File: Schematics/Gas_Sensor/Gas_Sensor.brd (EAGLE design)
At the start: 46.7 x 45.7 mm, 9 parts, among them J1 RJ45, X1 GAS_SENSOR

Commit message: Layout for final inspection
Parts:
- C1, C2: value (none) -> 0.1uF
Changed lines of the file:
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@@
 <layer number="25" name="tNames" color="7" fill="1" visible="yes" active="yes"/>
 <layer number="26" name="bNames" color="7" fill="1" visible="yes" active="yes"/>
-<layer number="27" name="tValues" color="7" fill="1" visible="yes" active="yes"/>
+<layer number="27" name="tValues" color="7" fill="1" visible="no" active="yes"/>
 <layer number="28" name="bValues" color="7" fill="1" visible="yes" active="yes"/>
 <layer number="29" name="tStop" color="7" fill="3" visible="no" active="yes"/>
@@
 </class>
 </classes>
-<designrules name="default">
+<designrules name="LaenPCBOrder">
 <description language="de">&lt;b&gt;EAGLE Design Rules&lt;/b&gt;
 &lt;p&gt;
@@
 Einstellungen hier und speichern die Design Rules unter
 einem neuen Namen ab.</description>
-<description language="en">&lt;b&gt;EAGLE Design Rules&lt;/b&gt;
+<description language="en">&lt;b&gt;Laen's PCB Order Design Rules&lt;/b&gt;
 &lt;p&gt;
-The default Design Rules have been set to cover
-a wide range of applications. Your particular design
-may have different requirements, so please make the
-necessary adjustments and save your customized
-design rules under a new name.</description>
+Please make sure your boards conform to these design rules.</description>
 <param name="layerSetup" value="(1*16)"/>
-<param name="mtCopper" value="0.035mm 0.035mm 0.035mm 0.035mm 0.035mm 0.035mm 0.035mm 0.035mm 0.035mm 0.035mm 0.035mm 0.035mm 0.035mm 0.035mm 0.035mm 0.035mm"/>
-<param name="mtIsolate" value="1.5mm 0.15mm 0.2mm 0.15mm 0.2mm 0.15mm 0.2mm 0.15mm 0.2mm 0.15mm 0.2mm 0.15mm 0.2mm 0.15mm 0.2mm"/>
-<param name="mdWireWire" value="8mil"/>
-<param name="mdWirePad" value="8mil"/>
-<param name="mdWireVia" value="8mil"/>
-<param name="mdPadPad" value="8mil"/>
-<param name="mdPadVia" value="8mil"/>
-<param name="mdViaVia" value="8mil"/>
-<param name="mdSmdPad" value="8mil"/>
-<param name="mdSmdVia" value="8mil"/>
-<param name="mdSmdSmd" value="8mil"/>
+<param name="mtCopper" value="0.0356mm 0.0356mm 0.0356mm 0.0356mm 0.0356mm 0.0356mm 0.0356mm 0.0356mm 0.0356mm 0.0356mm 0.0356mm 0.0356mm 0.0356mm 0.0356mm 0.0356mm 0.0356mm"/>
+<param name="mtIsolate" value="1.5011mm 0.1499mm 0.2007mm 0.1499mm 0.2007mm 0.1499mm 0.2007mm 0.1499mm 0.2007mm 0.1499mm 0.2007mm 0.1499mm 0.2007mm 0.1499mm 0.2007mm"/>
+<param name="mdWireWire" value="6mil"/>
+<param name="mdWirePad" value="6mil"/>
+<param name="mdWireVia" value="6mil"/>
+<param name="mdPadPad" value="6mil"/>
+<param name="mdPadVia" value="6mil"/>
+<param name="mdViaVia" value="6mil"/>
+<param name="mdSmdPad" value="6mil"/>
+<param name="mdSmdVia" value="6mil"/>
+<param name="mdSmdSmd" value="6mil"/>
 <param name="mdViaViaSameLayer" value="8mil"/>
 <param name="mnLayersViaInSmd" value="2"/>
-<param name="mdCopperDimension" value="40mil"/>
-<param name="mdDrill" value="8mil"/>
+<param name="mdCopperDimension" value="15mil"/>
+<param name="mdDrill" value="6mil"/>
 <param name="mdSmdStop" value="0mil"/>
-<param name="msWidth" value="10mil"/>
-<param name="msDrill" value="24mil"/>
-<param name="msMicroVia" value="9.99mm"/>
+<param name="msWidth" value="6mil"/>
+<param name="msDrill" value="13mil"/>
+<param name="msMicroVia" value="13mil"/>
 <param name="msBlindViaRatio" value="0.5"/>
 <param name="rvPadTop" value="0.25"/>
@@
 <param name="rvMicroViaOuter" value="0.25"/>
 <param name="rvMicroViaInner" value="0.25"/>
-<param name="rlMinPadTop" value="10mil"/>
+<param name="rlMinPadTop" value="7mil"/>
 <param name="rlMaxPadTop" value="20mil"/>
-<param name="rlMinPadInner" value="10mil"/>
+<param name="rlMinPadInner" value="7mil"/>
 <param name="rlMaxPadInner" value="20mil"/>
-<param name="rlMinPadBottom" value="10mil"/>
+<param name="rlMinPadBottom" value="7mil"/>
 <param name="rlMaxPadBottom" value="20mil"/>
-<param name="rlMinViaOuter" value="8mil"/>
+<param name="rlMinViaOuter" value="7mil"/>
 <param name="rlMaxViaOuter" value="20mil"/>
-<param name="rlMinViaInner" value="8mil"/>
+<param name="rlMinViaInner" value="7mil"/>
 <param name="rlMaxViaInner" value="20mil"/>
 <param name="rlMinMicroViaOuter" value="4mil"/>
@@
 <param name="mvStopFrame" value="1"/>
 <param name="mvCreamFrame" value="0"/>
-<param name="mlMinStopFrame" value="4mil"/>
-<param name="mlMaxStopFrame" value="4mil"/>
+<param name="mlMinStopFrame" value="3mil"/>
+<param name="mlMaxStopFrame" value="3mil"/>
 <param name="mlMinCreamFrame" value="0mil"/>
 <param name="mlMaxCreamFrame" value="0mil"/>
@@
 <element name="H2" library="holes" package="2,8" value="MOUNT-HOLE2.8" x="5.08" y="74.93"/>
 <element name="H3" library="holes" package="2,8" value="MOUNT-HOLE2.8" x="41.91" y="74.93"/>
-<element name="C1" library="rcl" package="C0603K" value="" x="24.765" y="59.055" smashed="yes">
+<element name="C1" library="rcl" package="C0603K" value="0.1uF" x="24.765" y="59.055" smashed="yes">
 <attribute name="NAME" x="26.505" y="57.8" size="1.016" layer="25"/>
 <attribute name="VALUE" x="23.965" y="57.405" size="1.016" layer="27"/>
 </element>
-<element name="C2" library="rcl" package="C0603K" value="" x="24.765" y="55.88" smashed="yes">
+<element name="C2" library="rcl" package="C0603K" value="0.1uF" x="24.765" y="55.88" smashed="yes">
 <attribute name="NAME" x="26.505" y="54.625" size="1.016" layer="25"/>
 <attribute name="VALUE" x="23.965" y="54.23" size="1.016" layer="27"/>

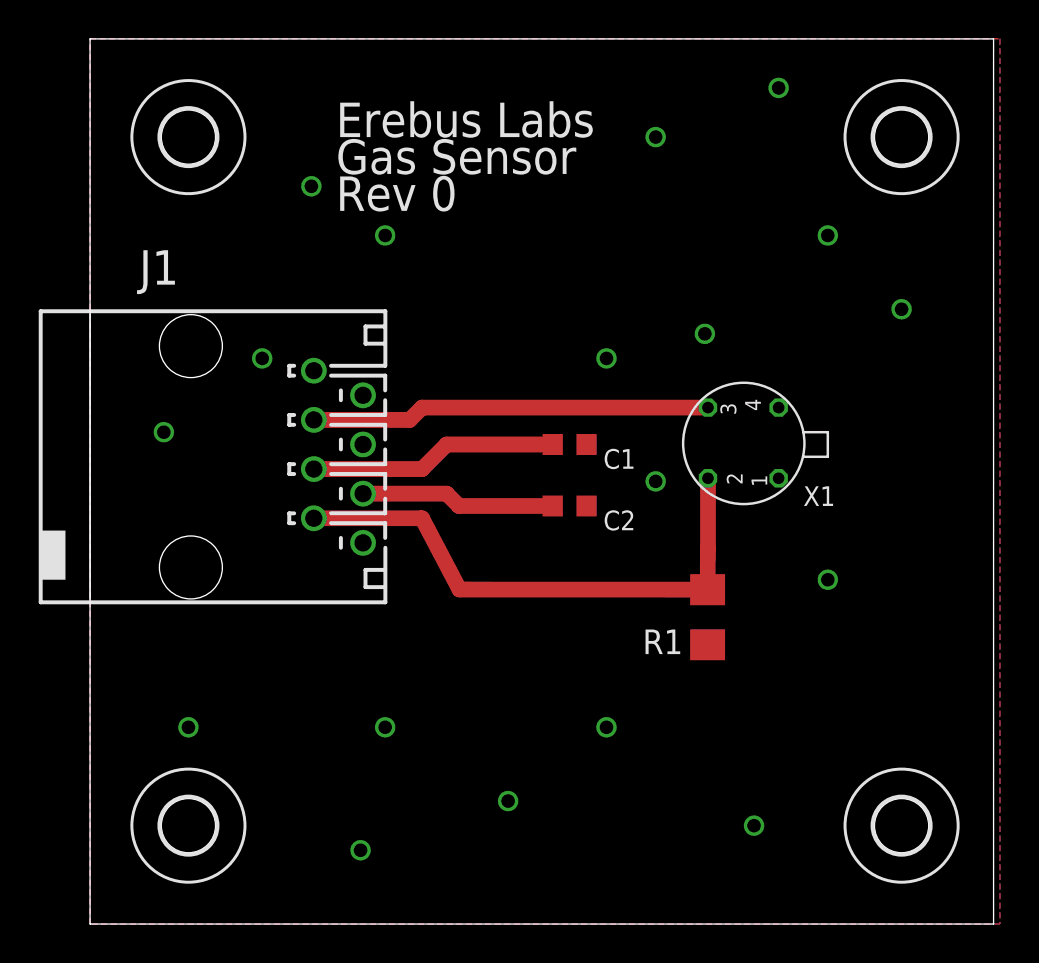
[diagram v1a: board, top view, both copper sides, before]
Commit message: Cleaned up stuff
Made Schematics easier to read
Split Supplies in BOM and made names match references
Renamed parts on sensor
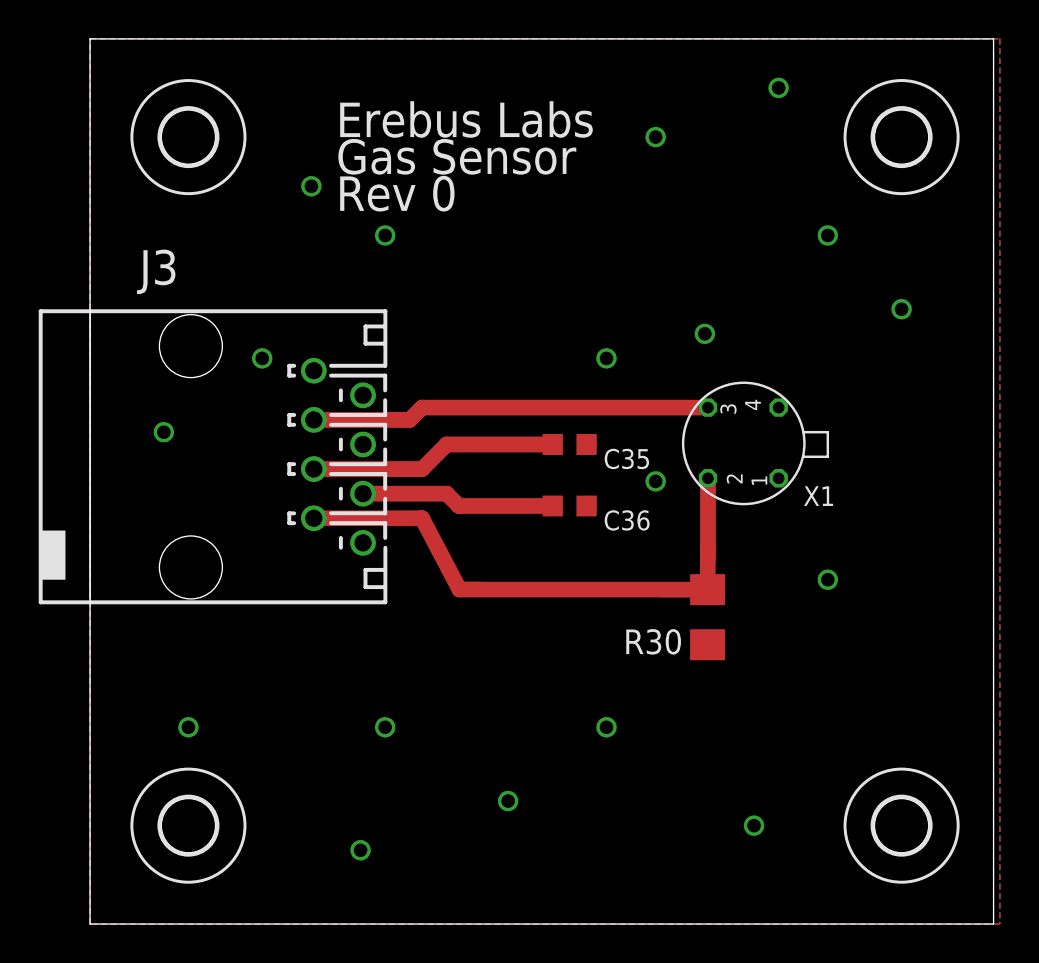
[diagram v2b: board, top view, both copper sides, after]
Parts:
- renumbered C1 to C35, C2 to C36, J1 to J3, R1 to R30
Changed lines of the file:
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@@
 <elements>
 <element name="X1" library="figaro" package="GAS_SENSOR" value="GAS_SENSOR" x="35.56" y="60.96" rot="R270"/>
-<element name="R1" library="rcl" package="R1206" value="30k" x="31.891640625" y="50.13414375" smashed="yes" rot="R90">
+<element name="R30" library="rcl" package="R1206" value="30k" x="31.891640625" y="50.13414375" smashed="yes" rot="R90">
 <attribute name="NAME" x="30.621640625" y="49.49914375" size="1.27" layer="25" rot="R180"/>
 <attribute name="VALUE" x="30.621640625" y="47.59414375" size="1.27" layer="27" rot="R180"/>
 </element>
-<element name="J1" library="con-amp" package="555167-1" value="RJ45" x="6.35" y="58.42" rot="R270"/>
+<element name="J3" library="con-amp" package="555167-1" value="RJ45" x="6.35" y="58.42" rot="R270"/>
 <element name="H4" library="holes" package="2,8" value="MOUNT-HOLE2.8" x="41.91" y="39.37"/>
 <element name="H1" library="holes" package="2,8" value="MOUNT-HOLE2.8" x="5.08" y="39.37"/>
 <element name="H2" library="holes" package="2,8" value="MOUNT-HOLE2.8" x="5.08" y="74.93"/>
 <element name="H3" library="holes" package="2,8" value="MOUNT-HOLE2.8" x="41.91" y="74.93"/>
-<element name="C1" library="rcl" package="C0603K" value="0.1uF" x="24.765" y="59.055" smashed="yes">
+<element name="C35" library="rcl" package="C0603K" value="0.1uF" x="24.765" y="59.055" smashed="yes">
 <attribute name="NAME" x="26.505" y="57.8" size="1.016" layer="25"/>
 <attribute name="VALUE" x="23.965" y="57.405" size="1.016" layer="27"/>
 </element>
-<element name="C2" library="rcl" package="C0603K" value="0.1uF" x="24.765" y="55.88" smashed="yes">
+<element name="C36" library="rcl" package="C0603K" value="0.1uF" x="24.765" y="55.88" smashed="yes">
 <attribute name="NAME" x="26.505" y="54.625" size="1.016" layer="25"/>
 <attribute name="VALUE" x="23.965" y="54.23" size="1.016" layer="27"/>
@@
 <signals>
 <signal name="AGND">
-<contactref element="R1" pad="1"/>
+<contactref element="R30" pad="1"/>
 <polygon width="0.4064" layer="16">
 <vertex x="0" y="80.01"/>
@@
 <vertex x="0" y="34.29"/>
 </polygon>
-<contactref element="J1" pad="1"/>
-<contactref element="J1" pad="2"/>
-<contactref element="C1" pad="2"/>
-<contactref element="C2" pad="2"/>
-<contactref element="J1" pad="4"/>
+<contactref element="J3" pad="1"/>
+<contactref element="J3" pad="2"/>
+<contactref element="C35" pad="2"/>
+<contactref element="C36" pad="2"/>
+<contactref element="J3" pad="4"/>
 <contactref element="X1" pad="P$1"/>
 <contactref element="X1" pad="P$2"/>
-<contactref element="J1" pad="8"/>
+<contactref element="J3" pad="8"/>
 <via x="13.97" y="38.1" extent="1-16" drill="0.7" diameter="0.4064"/>
 <via x="15.24" y="44.45" extent="1-16" drill="0.7" diameter="0.4064"/>
@@
 </signal>
 <signal name="N$2">
-<contactref element="R1" pad="2"/>
+<contactref element="R30" pad="2"/>
 <contactref element="X1" pad="P$4"/>
-<contactref element="J1" pad="7"/>
+<contactref element="J3" pad="7"/>
 <wire x1="31.91" y1="57.31" x2="31.91" y2="53.652" width="0.8128" layer="1"/>
 <wire x1="31.91" y1="53.652" x2="31.891640625" y2="51.55614375" width="0.8128" layer="1"/>
@@
 </signal>
 <signal name="N$25">
-<contactref element="J1" pad="5"/>
-<contactref element="C1" pad="1"/>
+<contactref element="J3" pad="5"/>
+<contactref element="C35" pad="1"/>
 <wire x1="11.557" y1="57.785" x2="17.145" y2="57.785" width="0.8128" layer="1"/>
 <wire x1="17.145" y1="57.785" x2="18.415" y2="59.055" width="0.8128" layer="1"/>
@@
 </signal>
 <signal name="N$24">
-<contactref element="J1" pad="6"/>
-<contactref element="C2" pad="1"/>
+<contactref element="J3" pad="6"/>
+<contactref element="C36" pad="1"/>
 <wire x1="14.097" y1="56.515" x2="18.415" y2="56.515" width="0.8128" layer="1"/>
 <wire x1="18.415" y1="56.515" x2="19.05" y2="55.88" width="0.8128" layer="1"/>
@@
 </signal>
 <signal name="N$26">
-<contactref element="J1" pad="3"/>
+<contactref element="J3" pad="3"/>
 <contactref element="X1" pad="P$3"/>
 <wire x1="11.557" y1="60.325" x2="16.51" y2="60.325" width="0.8128" layer="1"/>

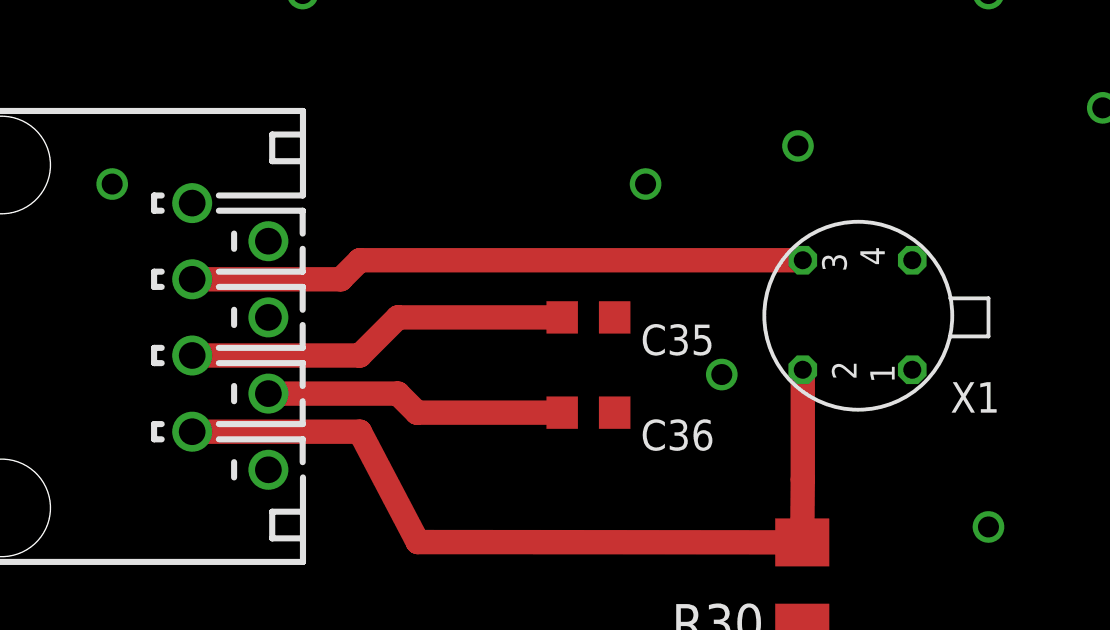
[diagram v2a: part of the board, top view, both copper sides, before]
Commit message: Boo Boo fix on Gas Sensor
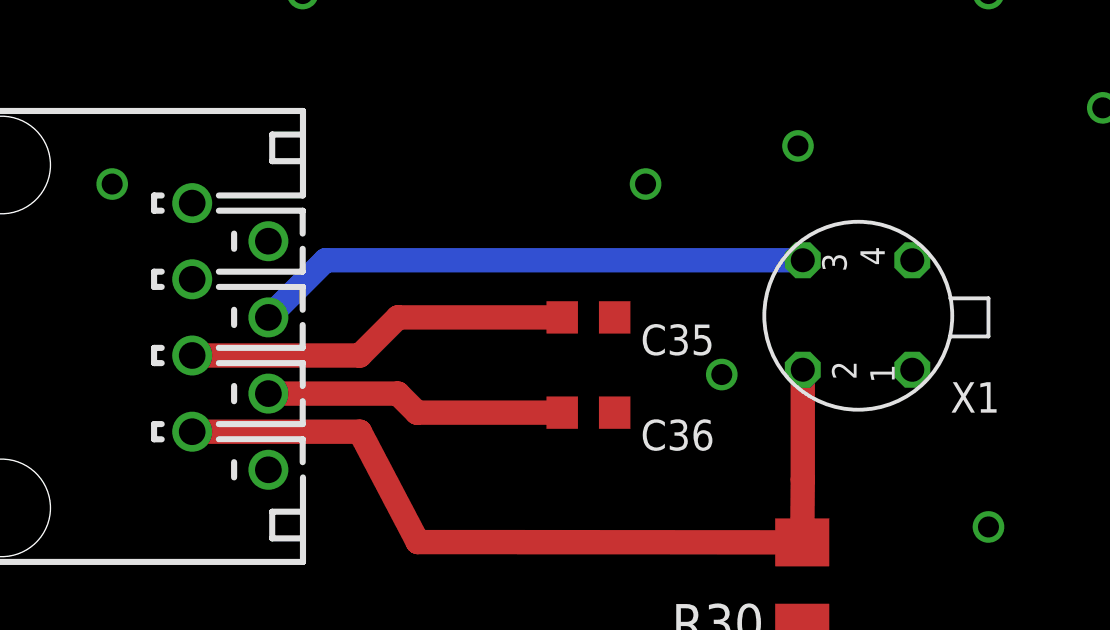
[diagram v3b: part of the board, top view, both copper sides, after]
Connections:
- removed net N$26: J3.3, X1.P$3
- new net N$1: J3.4, X1.P$3
- net AGND: now also J3.3; no longer J3.4
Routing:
- net N$26: track 20.6 -> 0.00 mm
- net N$1: track 0.00 -> 18.6 mm
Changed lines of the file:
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@@
 <contactref element="C35" pad="2"/>
 <contactref element="C36" pad="2"/>
-<contactref element="J3" pad="4"/>
 <contactref element="X1" pad="P$1"/>
 <contactref element="X1" pad="P$2"/>
@@
 <via x="15.24" y="69.85" extent="1-16" drill="0.7" diameter="0.4064"/>
 <via x="11.43" y="72.39" extent="1-16" drill="0.7" diameter="0.4064"/>
+<contactref element="J3" pad="3"/>
 </signal>
 <signal name="N$2">
@@
 <wire x1="19.05" y1="55.88" x2="23.89" y2="55.88" width="0.8128" layer="1"/>
 </signal>
-<signal name="N$26">
-<contactref element="J3" pad="3"/>
+<signal name="N$1">
+<contactref element="J3" pad="4"/>
 <contactref element="X1" pad="P$3"/>
-<wire x1="11.557" y1="60.325" x2="16.51" y2="60.325" width="0.8128" layer="1"/>
-<wire x1="16.51" y1="60.325" x2="17.145" y2="60.96" width="0.8128" layer="1"/>
-<wire x1="17.145" y1="60.96" x2="31.91" y2="60.96" width="0.8128" layer="1"/>
+<wire x1="31.91" y1="60.96" x2="16.002" y2="60.96" width="0.8128" layer="16"/>
+<wire x1="16.002" y1="60.96" x2="14.097" y2="59.055" width="0.8128" layer="16"/>
 </signal>
 </signals>
